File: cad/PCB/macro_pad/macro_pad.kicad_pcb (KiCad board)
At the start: 2 copper layers, 82.3 x 100.8 mm, 39 parts, among them SW1 SW_Push, SW10 SW_Push, SW11 SW_Push, SW12 SW_Push, SW13 SW_Push, SW14 SW_Push, SW15 SW_Push, SW16 SW_Push, SW17 RotaryEncoder_Switch, SW2 SW_Push, SW3 SW_Push, SW4 SW_Push, SW5 SW_Push, SW6 SW_Push, SW7 SW_Push, SW8 SW_Push, SW9 SW_Push, U1 XIAO-SAMD21-DIP

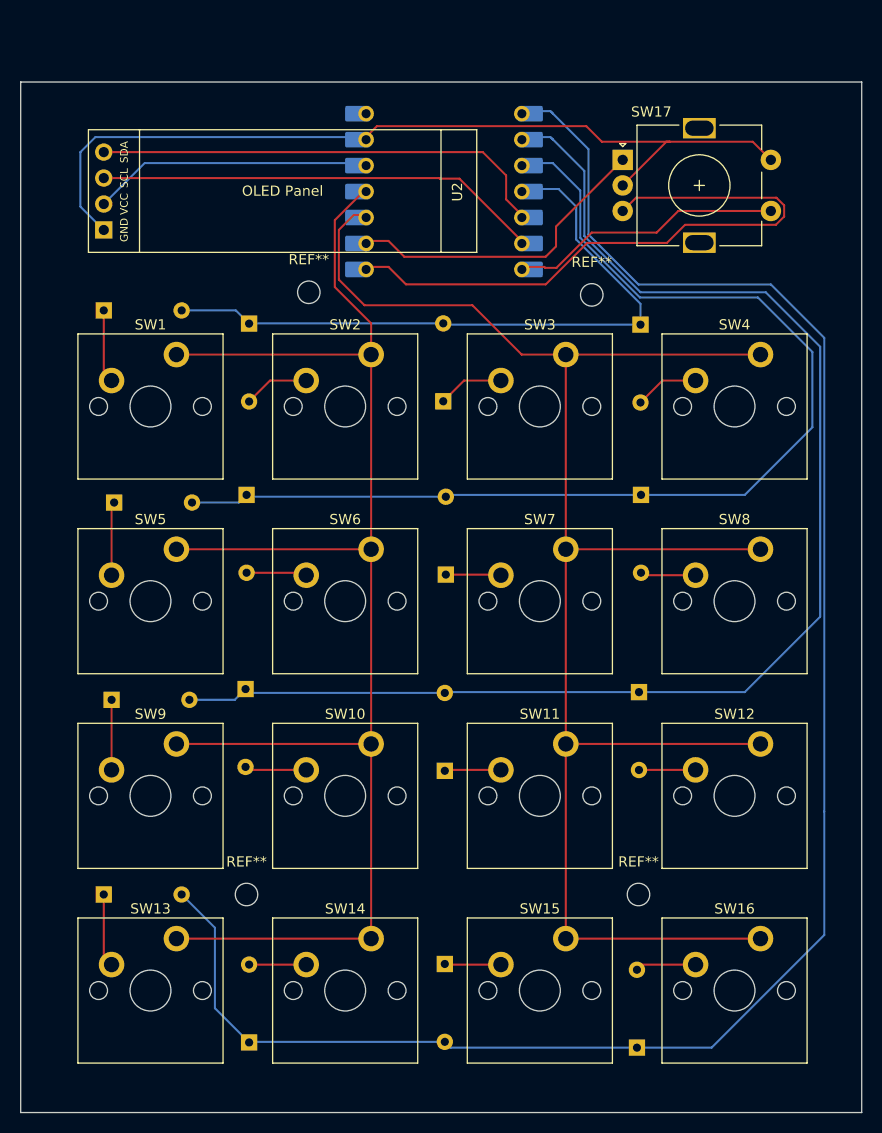
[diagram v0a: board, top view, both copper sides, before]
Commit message: moved encoder and mcu
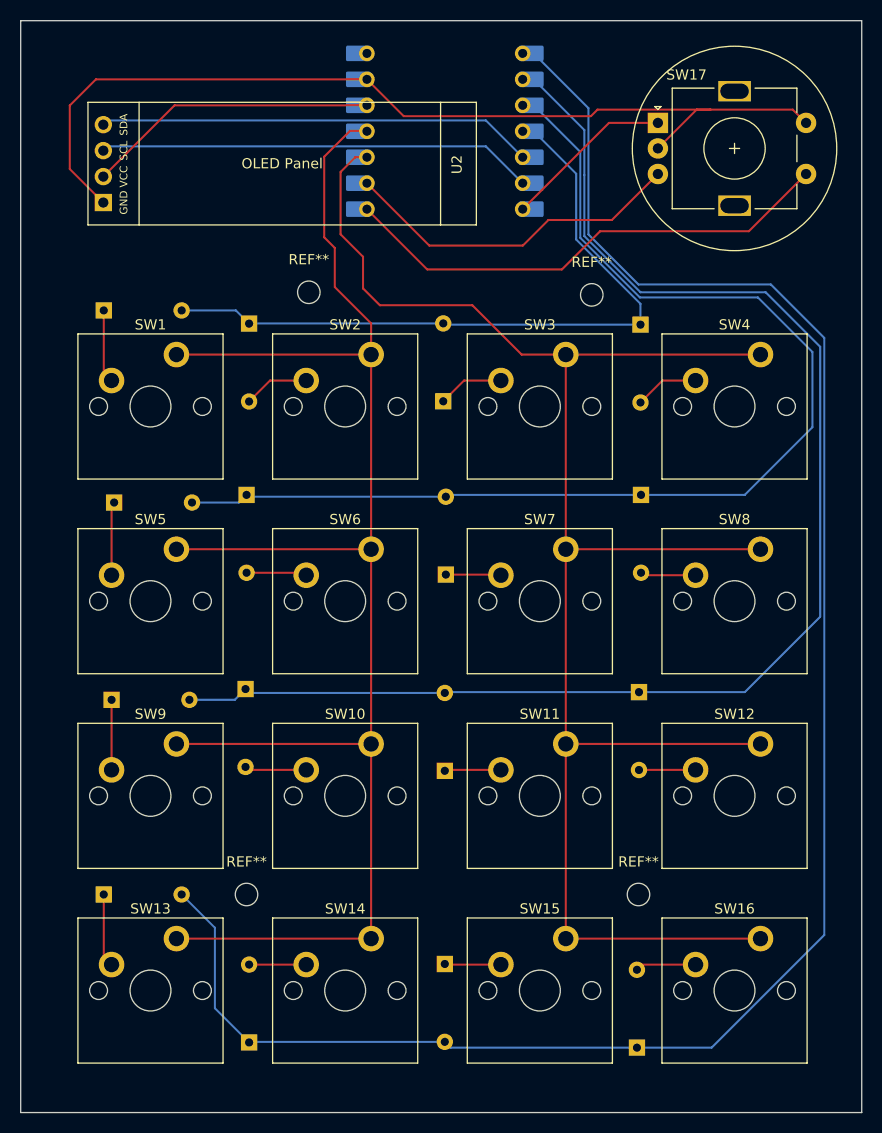
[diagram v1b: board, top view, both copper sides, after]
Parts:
- moved U1 5.90 mm to (143.0, 68.3)
- moved SW17 5.00 mm to (163.9, 67.5)
- moved U2 2.68 mm to (146.2, 77.5)
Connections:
- SW17 pad A: Net-(U1-PA7_A8_D8_SCK) -> Net-(U1-PB08_A6_D6_TX)
- SW17 pad B: Net-(U1-PB09_A7_D7_RX) -> Net-(U1-PA7_A8_D8_SCK)
- SW17 pad S1: Net-(U1-PB08_A6_D6_TX) -> Net-(U1-PB09_A7_D7_RX)
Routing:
- net Net-(U1-PB09_A7_D7_RX): track 62.1 -> 49.3 mm
- net Net-(U1-PB08_A6_D6_TX): track 26.7 -> 17.4 mm
- net /GND: track 84.1 -> 93.0 mm
- net Net-(U1-PA6_A10_D10_MOSI): track 152.3 -> 159.8 mm
- net Net-(U1-PA5_A9_D9_MISO): track 166.7 -> 171.4 mm
- net Net-(D5-A): track 110.1 -> 114.5 mm
- net Net-(D10-K): track 133.4 -> 137.9 mm
- net Net-(D13-A): track 180.8 -> 185.2 mm
- net Net-(D1-A): track 65.8 -> 69.9 mm
- net Net-(U1-PA7_A8_D8_SCK): track 30.8 -> 33.9 mm
- net Net-(U1-PA8_A4_D4_SDA): track 44.9 -> 42.7 mm
- net /Vcc: track 27.3 -> 28.7 mm
- net Net-(U1-PA9_A5_D5_SCL): track 43.4 -> 42.7 mm
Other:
- board size 82.3 x 100.8 mm -> 82.3 x 106.8 mm

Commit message: modified shape of pcb
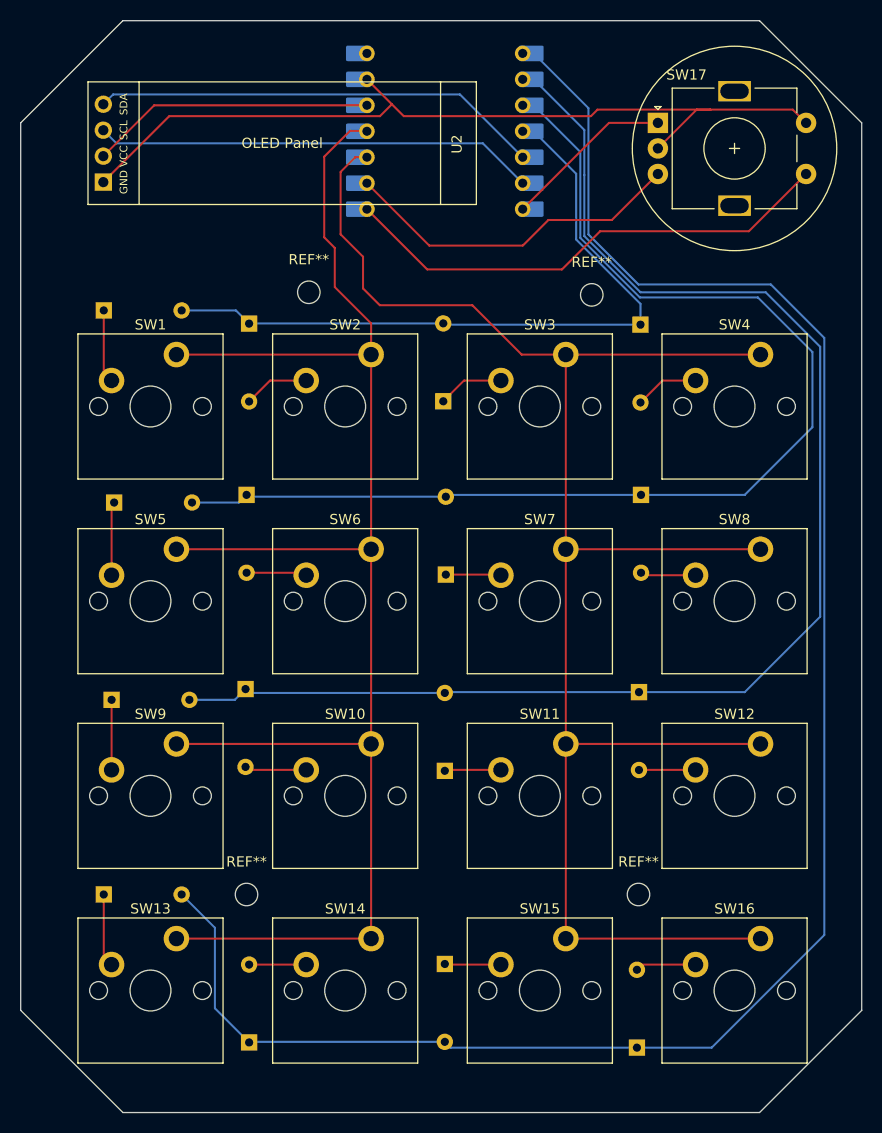
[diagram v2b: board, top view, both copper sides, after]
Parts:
- moved U2 2.00 mm to (146.2, 75.5)
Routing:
- net /GND: track 93.0 -> 83.4 mm
- net Net-(U1-PA8_A4_D4_SDA): track 42.7 -> 44.0 mm
- net /Vcc: track 28.7 -> 27.9 mm
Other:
- outline, holes or cut-outs redrawn
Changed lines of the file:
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@@
 	(footprint "Downloads:SSD1306-0.91-OLED-4pin-128x32"
 		(layer "F.Cu")
-		(at 146.185 77.485 180)
+		(at 146.185 75.485 180)
 		(property "Reference" "U2"
 			(at 1.9 5.91 90)
@@
 		(layer "F.SilkS")
 	)
-	(gr_rect
-		(start 101.6 57.5)
-		(end 183.896 164.338)
+	(gr_line
+		(start 111.6 57.5)
+		(end 173.896 57.5)
+		(stroke
+			(width 0.05)
+			(type default)
+		)
+		(layer "Edge.Cuts")
+	)
+	(gr_line
+		(start 183.896 67.5)
+		(end 183.896 154.338)
+		(stroke
+			(width 0.05)
+			(type default)
+		)
+		(layer "Edge.Cuts")
+	)
+	(gr_line
+		(start 101.6 67.5)
+		(end 101.6 154.338)
+		(stroke
+			(width 0.05)
+			(type default)
+		)
+		(layer "Edge.Cuts")
+	)
+	(gr_line
+		(start 101.6 154.338)
+		(end 111.6 164.338)
+		(stroke
+			(width 0.05)
+			(type default)
+		)
+		(layer "Edge.Cuts")
+	)
+	(gr_line
+		(start 183.896 154.338)
+		(end 173.896 164.338)
 		(stroke
 			(width 0.05)
 			(type default)
 		)
-		(fill none)
 		(layer "Edge.Cuts")
 	)
+	(gr_line
+		(start 111.6 164.338)
+		(end 173.896 164.338)
+		(stroke
+			(width 0.05)
+			(type default)
+		)
+		(layer "Edge.Cuts")
+	)
+	(gr_line
+		(start 183.896 67.5)
+		(end 173.896 57.5)
+		(stroke
+			(width 0.05)
+			(type default)
+		)
+		(layer "Edge.Cuts")
+	)
+	(gr_line
+		(start 101.6 67.5)
+		(end 111.6 57.5)
+		(stroke
+			(width 0.05)
+			(type default)
+		)
+		(layer "Edge.Cuts")
+	)
+	(gr_line
+		(start 183.9 164.3)
+		(end 183.9 154.3)
+		(stroke
+			(width 0.1)
+			(type default)
+		)
+		(layer "User.1")
+	)
 	(segment
 		(start 162.248 85.205058)
@@
 	)
 	(segment
-		(start 108.96 63.24)
-		(end 135.48 63.24)
+		(start 157.4 66.842)
+		(end 139.082 66.842)
 		(width 0.2)
 		(layer "F.Cu")
@@
 	)
 	(segment
-		(start 157.4 66.842)
-		(end 139.082 66.842)
+		(start 109.73 72.9)
+		(end 109.728 72.898)
 		(width 0.2)
 		(layer "F.Cu")
@@
 	)
 	(segment
-		(start 109.685 75.295)
-		(end 106.4 72.01)
-		(width 0.2)
-		(layer "F.Cu")
-		(net 22)
-	)
-	(segment
 		(start 169.1 66.2)
 		(end 158.042 66.2)
@@
 	)
 	(segment
-		(start 139.082 66.842)
+		(start 137.92 65.68)
 		(end 135.48 63.24)
 		(width 0.2)
@@
 	)
 	(segment
-		(start 106.4 72.01)
-		(end 106.4 65.8)
+		(start 136.758 66.842)
+		(end 137.92 65.68)
 		(width 0.2)
 		(layer "F.Cu")
@@
 	)
 	(segment
+		(start 139.082 66.842)
+		(end 137.92 65.68)
+		(width 0.2)
+		(layer "F.Cu")
+		(net 22)
+	)
+	(segment
 		(start 158.042 66.2)
 		(end 157.4 66.842)
@@
 	)
 	(segment
-		(start 106.4 65.8)
-		(end 108.96 63.24)
+		(start 109.685 73.295)
+		(end 116.138 66.842)
+		(width 0.2)
+		(layer "F.Cu")
+		(net 22)
+	)
+	(segment
+		(start 116.138 66.842)
+		(end 136.758 66.842)
 		(width 0.2)
 		(layer "F.Cu")
@@
 	)
 	(segment
-		(start 109.685 72.755)
-		(end 116.66 65.78)
-		(width 0.2)
-		(layer "F.Cu")
-		(net 25)
-	)
-	(segment
-		(start 116.66 65.78)
+		(start 114.66 65.78)
 		(end 135.48 65.78)
 		(width 0.2)
@@
 	)
 	(segment
-		(start 109.73 72.9)
-		(end 109.728 72.898)
+		(start 109.685 70.755)
+		(end 114.66 65.78)
 		(width 0.2)
 		(layer "F.Cu")
@@
 	)
 	(segment
-		(start 110.102 67.258)
-		(end 147.118 67.258)
+		(start 144.578 64.718)
+		(end 150.72 70.86)
 		(width 0.2)
 		(layer "B.Cu")
@@
 	)
 	(segment
-		(start 147.118 67.258)
-		(end 150.72 70.86)
+		(start 109.685 65.675)
+		(end 110.642 64.718)
 		(width 0.2)
 		(layer "B.Cu")
@@
 	)
 	(segment
-		(start 109.685 67.675)
-		(end 110.102 67.258)
+		(start 110.642 64.718)
+		(end 144.578 64.718)
 		(width 0.2)
 		(layer "B.Cu")
@@
 	)
 	(segment
-		(start 109.685 70.215)
-		(end 110.102 69.798)
+		(start 109.685 68.215)
+		(end 110.97 69.5)
 		(width 0.2)
 		(layer "B.Cu")
@@
 	)
 	(segment
-		(start 110.102 69.798)
-		(end 147.118 69.798)
+		(start 146.82 69.5)
+		(end 150.72 73.4)
 		(width 0.2)
 		(layer "B.Cu")
@@
 	)
 	(segment
-		(start 147.118 69.798)
-		(end 150.72 73.4)
+		(start 110.97 69.5)
+		(end 146.82 69.5)
 		(width 0.2)
 		(layer "B.Cu")
